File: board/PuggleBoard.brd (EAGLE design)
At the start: 54.6 x 86.4 mm, 140 parts, among them U1 OPA4209, U10 24C, U2 ADS8331, U3 AD5686, U4 OPA4209, U5 TPS7A3001, U6 TPS7A4901, U7 LTM8045, U8 REF5040, U9 AD8032

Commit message: Fixed several problems in grounding scheme causing digital/analog interference.
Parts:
- moved C16 3.61 mm to (7.87, 65.5), turned to 90 degrees
- moved C3 1.42 mm to (17.1, 42.7), turned to 180 degrees
- moved C4 1.25 mm to (16.9, 44.5), turned to 180 degrees
- moved C15 0.65 mm to (17.8, 63.6), turned to 270 degrees
- moved C1 0.57 mm to (10.7, 42.4), turned to 180 degrees
- moved C14 0.40 mm to (19.6, 63.9), turned to 270 degrees
- moved C2 0.13 mm to (10.8, 44.2), turned to 180 degrees
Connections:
- net +4.5V renamed N$27
- removed net DGND: BB1.48
- net GND: now also BB1.48
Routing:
- net VDRIVE: track 54.3 -> 26.1 mm
- net DGND: track 24.2 -> 0.00 mm, vias 1 -> 0
- net N$31: track 75.2 -> 65.7 mm
- net N$35: track 68.1 -> 60.5 mm
- net GND: track 117.9 -> 114.7 mm, vias 82 -> 84
- net DAC_+IN_C: track 37.4 -> 35.9 mm
- net N$27: track 42.5 -> 41.7 mm, vias 15 -> 16
- net SPI4: track 23.2 -> 23.8 mm
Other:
- board text added: "PuggleBoard v2.1 Aug. 2013"
- board text removed: "PuggleBoard v2.0 Aug. 2013"

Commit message: Fixed V_Ref bypass cap for DAC.
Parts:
- C21: value 0.1uF -> 10uF; device puggleboard:0603 -> puggleboard:0805
- moved C21 0.36 mm to (19.1, 59.3)

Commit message: Almost done with 2v0 board changes. Getting ready for 2.1 fabrication.
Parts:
- added C46: 22uF, puggleboard:1206
- U1: value OPA4209 -> LMP7704
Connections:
- net GND: now also C46.1
- net VDRIVE: now also C46.2
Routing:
- net GND: track 115.1 -> 116.6 mm, vias 84 -> 85
- net VDRIVE: track 26.1 -> 27.6 mm, vias 14 -> 15
- net N$20: track 12.9 -> 12.0 mm

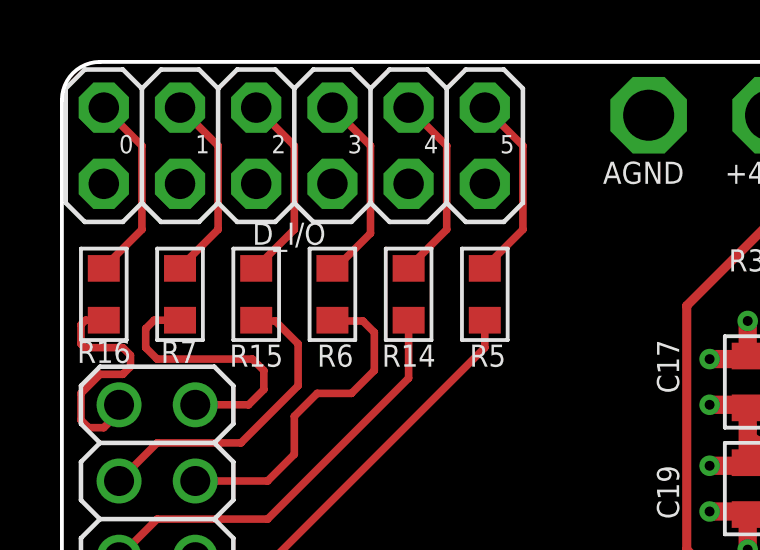
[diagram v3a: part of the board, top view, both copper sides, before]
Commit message: Changes to ground/vdrive planes.
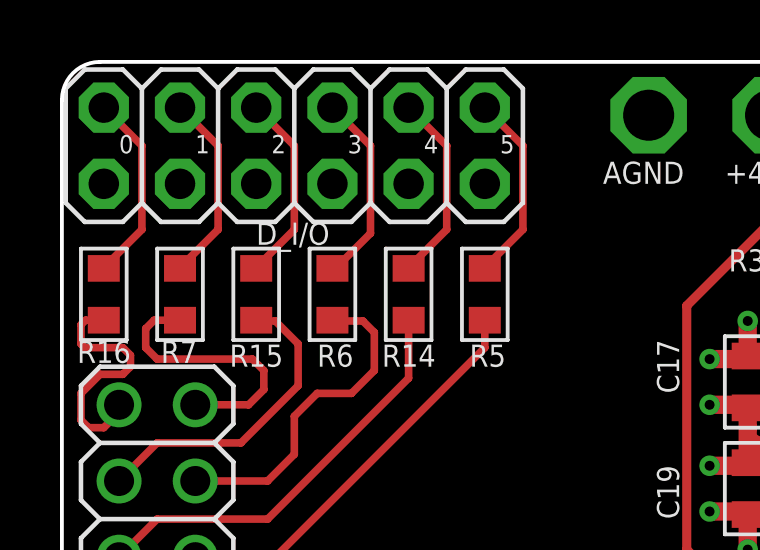
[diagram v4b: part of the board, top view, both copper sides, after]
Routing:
- net -4.5V: track 88.9 -> 88.2 mm
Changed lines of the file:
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@@
 </element>
 <element name="D_I/O" library="puggleboard" package="2X06" value="PINHD-2X6" x="7.747" y="83.566" smashed="yes">
-<attribute name="NAME" x="6.35" y="80.264" size="0.7366" layer="25" font="vector" ratio="12"/>
+<attribute name="NAME" x="6.477" y="80.264" size="0.7366" layer="25" font="vector" ratio="12"/>
 </element>
 <element name="U$1" library="puggleboard" package="PB-LOGO" value="" x="41.529" y="6.985"/>
@@
 <wire x1="44.45" y1="37.338" x2="47.625" y2="37.338" width="0.8128" layer="15"/>
 <wire x1="47.625" y1="37.338" x2="48.514" y2="38.354" width="0.8128" layer="15"/>
-<wire x1="48.514" y1="79.248" x2="47.879" y2="79.883" width="0.8128" layer="15"/>
-<wire x1="47.879" y1="79.883" x2="47.244" y2="80.518" width="0.8128" layer="15"/>
+<wire x1="48.514" y1="79.248" x2="47.752" y2="80.01" width="0.8128" layer="15"/>
+<wire x1="47.752" y1="80.01" x2="47.244" y2="80.518" width="0.8128" layer="15"/>
 <wire x1="47.244" y1="80.518" x2="43.053" y2="80.518" width="0.8128" layer="15"/>
 <via x="45.466" y="37.338" extent="1-16" drill="0.3302"/>
 <via x="46.482" y="37.338" extent="1-16" drill="0.3302"/>
-<wire x1="40.64" y1="80.518" x2="35.56" y2="80.518" width="0.8128" layer="15"/>
+<wire x1="40.64" y1="80.518" x2="36.322" y2="80.518" width="0.8128" layer="15"/>
+<wire x1="36.322" y1="80.518" x2="35.052" y2="79.248" width="0.8128" layer="15"/>
 <via x="34.29" y="72.898" extent="1-16" drill="0.3302"/>
 <via x="34.29" y="74.93" extent="1-16" drill="0.3302"/>
@@
 <wire x1="33.108" y1="72.898" x2="34.29" y2="72.898" width="0.6096" layer="1"/>
 <wire x1="34.29" y1="74.93" x2="33.02" y2="74.93" width="0.6096" layer="1"/>
-<wire x1="49.022" y1="81.788" x2="49.276" y2="81.28" width="0.3048" layer="15"/>
-<wire x1="49.276" y1="81.28" x2="47.879" y2="79.883" width="0.3048" layer="15"/>
 <via x="48.514" y="74.93" extent="1-16" drill="0.3302"/>
 <via x="48.514" y="72.898" extent="1-16" drill="0.3302"/>
@@
 <wire x1="40.64" y1="80.518" x2="43.053" y2="80.518" width="0.8128" layer="16"/>
 <via x="35.052" y="79.248" extent="1-16" drill="0.6"/>
-<wire x1="35.56" y1="80.518" x2="35.052" y2="80.01" width="0.8128" layer="15"/>
-<wire x1="35.052" y1="80.01" x2="35.052" y2="79.248" width="0.8128" layer="15"/>
 <wire x1="35.052" y1="79.248" x2="34.29" y2="78.486" width="0.8128" layer="16"/>
 <wire x1="34.29" y1="78.486" x2="34.29" y2="74.93" width="0.8128" layer="16"/>
 <wire x1="34.29" y1="74.93" x2="34.29" y2="72.898" width="0.8128" layer="16"/>
+<wire x1="49.022" y1="81.788" x2="49.022" y2="81.28" width="0.4064" layer="15"/>
+<wire x1="49.022" y1="81.28" x2="47.752" y2="80.01" width="0.4064" layer="15"/>
 </signal>
 <signal name="VDRIVE">
@@
 <vertex x="0" y="86.106"/>
 <vertex x="0.254" y="86.36"/>
-<vertex x="15.748" y="86.36"/>
-<vertex x="15.748" y="68.072"/>
-<vertex x="12.7" y="65.024"/>
+<vertex x="16.002" y="86.36"/>
+<vertex x="16.002" y="64.897"/>
+<vertex x="13.6919" y="64.897"/>
+<vertex x="12.7" y="63.9051"/>
 <vertex x="12.7" y="55.372"/>
 <vertex x="13.97" y="53.975"/>
@@
 <via x="27.051" y="22.479" extent="1-16" drill="0.6"/>
 <contactref element="C46" pad="2"/>
-<wire x1="8.382" y1="26.3144" x2="8.382" y2="26.162" width="0" layer="19" extent="1-1"/>
 <wire x1="27.051" y1="22.479" x2="25.527" y2="22.479" width="1.016" layer="1"/>
+<wire x1="8.382" y1="26.162" x2="8.382" y2="26.3144" width="0" layer="19" extent="1-1"/>
 </signal>
 <signal name="VDD_5V">
@@
 <polygon width="0.254" layer="2" thermals="no">
 <vertex x="0.127" y="86.36"/>
+<vertex x="16.002" y="86.36"/>
+<vertex x="16.002" y="73.406"/>
+<vertex x="10.549153125" y="67.953153125" curve="135"/>
+<vertex x="10.710346875" y="67.564" curve="44.999782"/>
+<vertex x="11.121625" y="67.73435625"/>
+<vertex x="16.637" y="73.24973125"/>
+<vertex x="16.637" y="86.36"/>
 <vertex x="46.001321875" y="86.36"/>
 <vertex x="49.022" y="83.339321875"/>
@@
 <vertex x="54.61" y="0"/>
 <vertex x="33.655" y="0"/>
-<vertex x="33.655" y="18.161"/>
-<vertex x="47.498" y="18.161"/>
+<vertex x="33.655" y="18.034"/>
+<vertex x="47.625" y="18.034"/>
 <vertex x="49.022" y="16.637"/>
 <vertex x="51.308" y="16.637"/>
@@
 <vertex x="27.305" y="37.973"/>
 <vertex x="17.399" y="37.973"/>
-<vertex x="15.24" y="40.132"/>
-<vertex x="15.113" y="40.132"/>
-<vertex x="14.732" y="39.751"/>
-<vertex x="14.732" y="39.624"/>
+<vertex x="15.405453125" y="39.966546875" curve="90"/>
+<vertex x="14.947546875" y="39.966546875" curve="90"/>
+<vertex x="14.947546875" y="39.408453125"/>
 <vertex x="17.018" y="37.338"/>
 <vertex x="27.051" y="37.338"/>
@@
 <vertex x="50.673" y="17.526"/>
 <vertex x="49.022" y="17.526"/>
-<vertex x="47.879" y="18.796"/>
+<vertex x="47.752" y="18.796"/>
 <vertex x="33.655" y="18.796"/>
 <vertex x="33.655" y="20.32"/>
@@
 <via x="20.701" y="22.479" extent="1-16" drill="0.6"/>
 <contactref element="C46" pad="1"/>
+<wire x1="20.701" y1="22.479" x2="22.225" y2="22.479" width="1.016" layer="1"/>
 <wire x1="52.705" y1="72.39" x2="52.705" y2="74.93" width="0" layer="19" extent="1-1"/>
 <wire x1="50.165" y1="74.93" x2="52.705" y2="74.93" width="0" layer="19" extent="1-1"/>
@@
 <wire x1="9.8806" y1="65.024" x2="9.906" y2="65.024" width="0" layer="19" extent="1-1"/>
 <wire x1="46.99" y1="71.2724" x2="46.99" y2="71.374" width="0" layer="19" extent="1-1"/>
-<wire x1="20.701" y1="22.479" x2="22.225" y2="22.479" width="1.016" layer="1"/>
 </signal>
 <signal name="BAT_SENSE">
@@
 <wire x1="43.942" y1="57.658" x2="44.196" y2="57.912" width="0.6096" layer="1"/>
 <polygon width="0.254" layer="15" thermals="no">
-<vertex x="16.256" y="86.36"/>
+<vertex x="16.637" y="86.36"/>
 <vertex x="46.001321875" y="86.36"/>
 <vertex x="49.022" y="83.339321875"/>
@@
 <vertex x="26.76168125" y="39.979434375"/>
 <vertex x="15.138565625" y="39.979434375"/>
-<vertex x="14.478" y="40.64"/>
-<vertex x="14.478" y="43.815"/>
+<vertex x="14.351" y="40.767"/>
+<vertex x="14.351" y="43.942"/>
 <vertex x="12.192" y="46.228"/>
 <vertex x="12.192" y="49.53"/>
@@
 <vertex x="14.478" y="54.102"/>
 <vertex x="13.208" y="55.499"/>
-<vertex x="13.208" y="64.77"/>
-<vertex x="16.256" y="67.818"/>
+<vertex x="13.208" y="63.70280625"/>
+<vertex x="13.89419375" y="64.389"/>
+<vertex x="16.637" y="64.389"/>
 </polygon>
 <wire x1="44.577" y1="57.023" x2="44.196" y2="56.642" width="0.6096" layer="1"/>

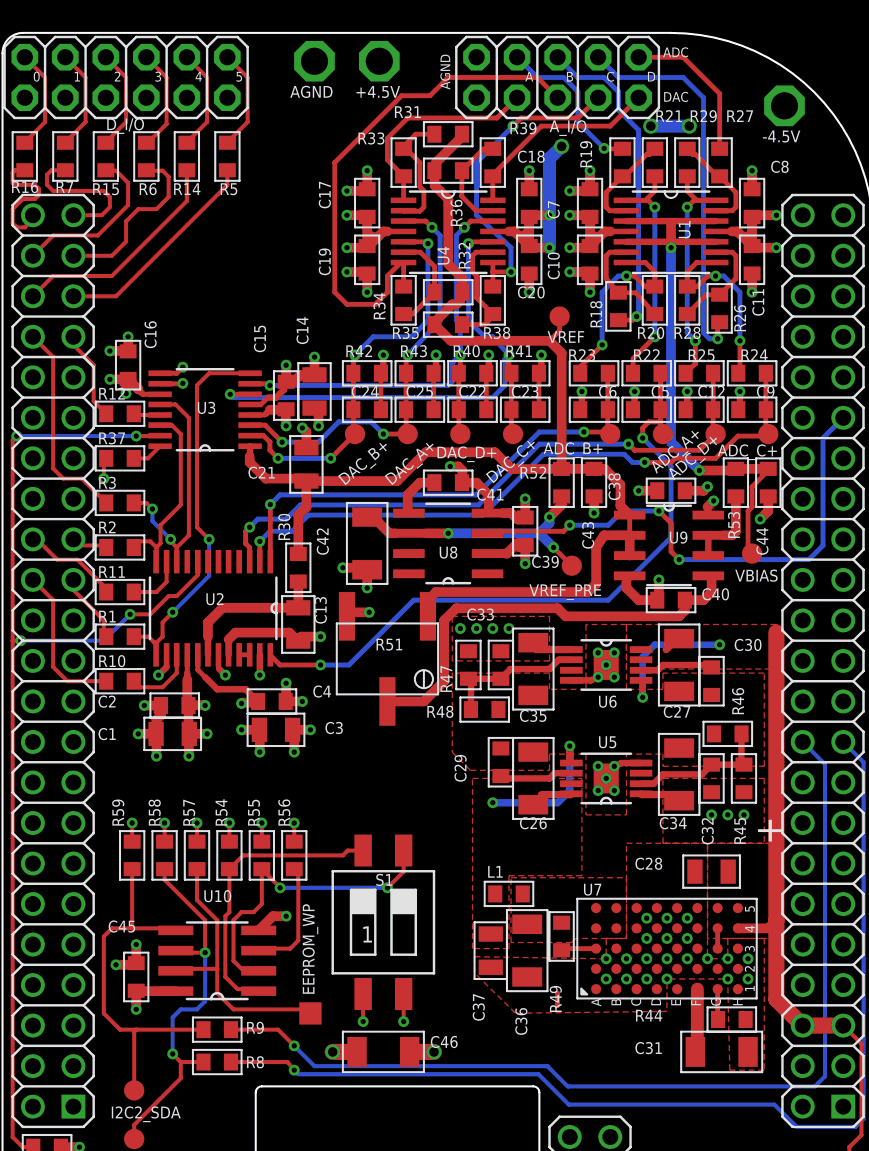
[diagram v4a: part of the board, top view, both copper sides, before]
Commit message: PuggleBoard version 2.1. Created gerbers and placed order.
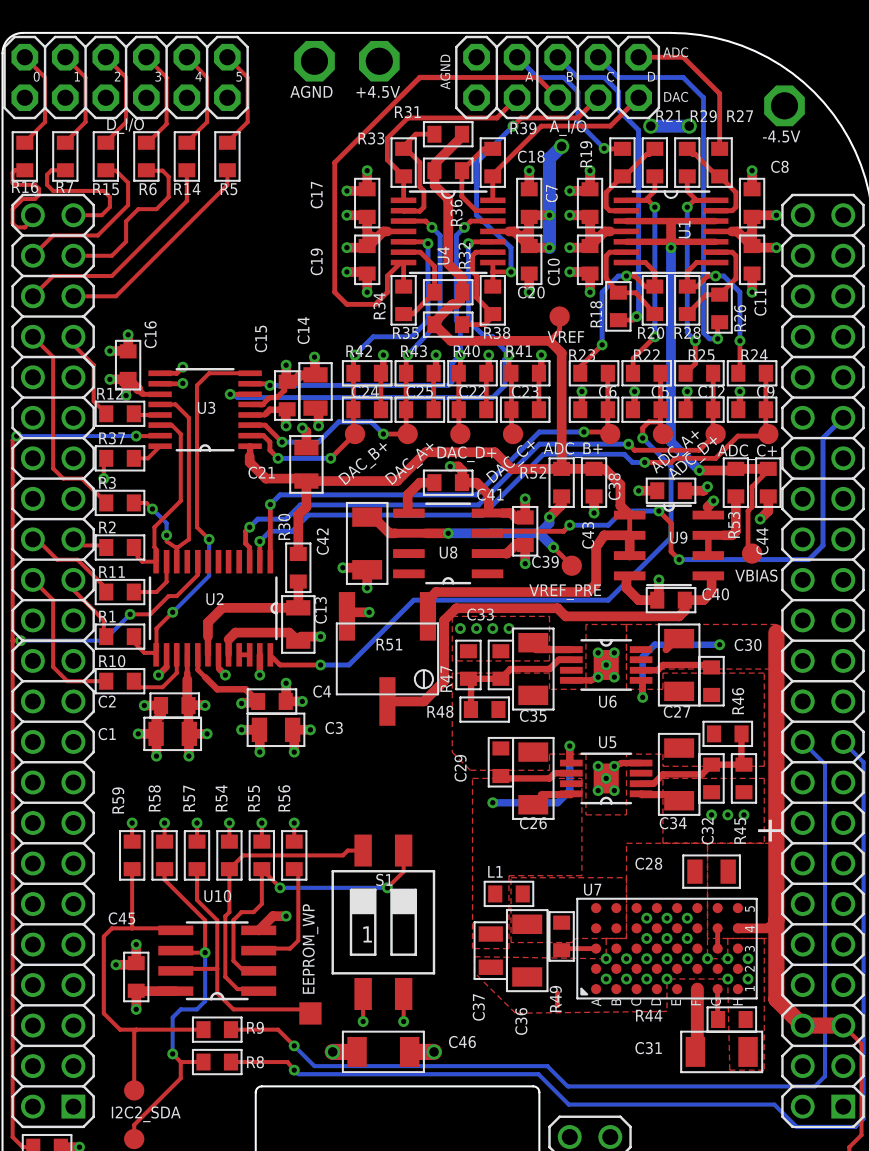
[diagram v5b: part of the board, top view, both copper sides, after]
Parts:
- moved U$2 2.67 mm to (31.2, 27.3)
- moved C14 0.06 mm to (19.6, 63.9)
- moved C15 0.06 mm to (17.8, 63.6)
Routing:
- net SPI3: track 12.1 -> 13.1 mm

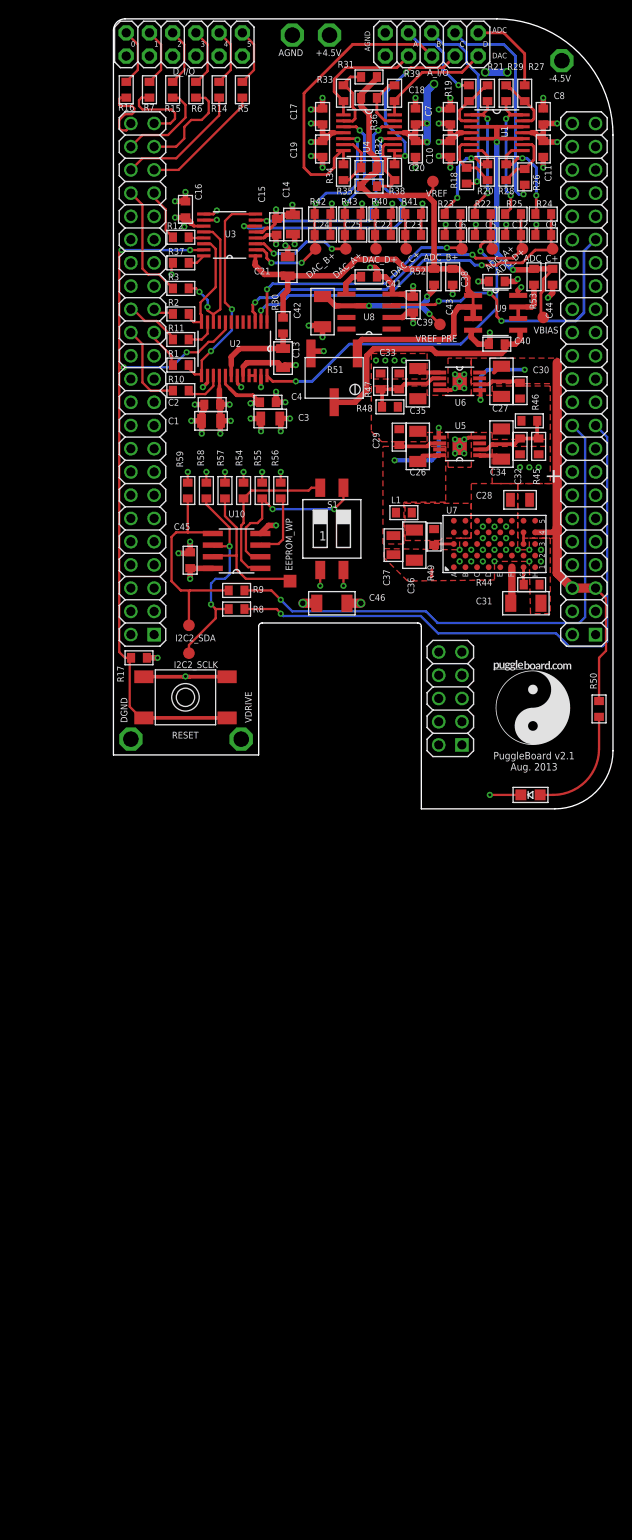
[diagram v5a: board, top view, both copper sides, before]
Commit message: Started fixing issues with r2.1 build. Fixed up silkscreen to make it more legible. Fixed issue with voltage ref miswiring.
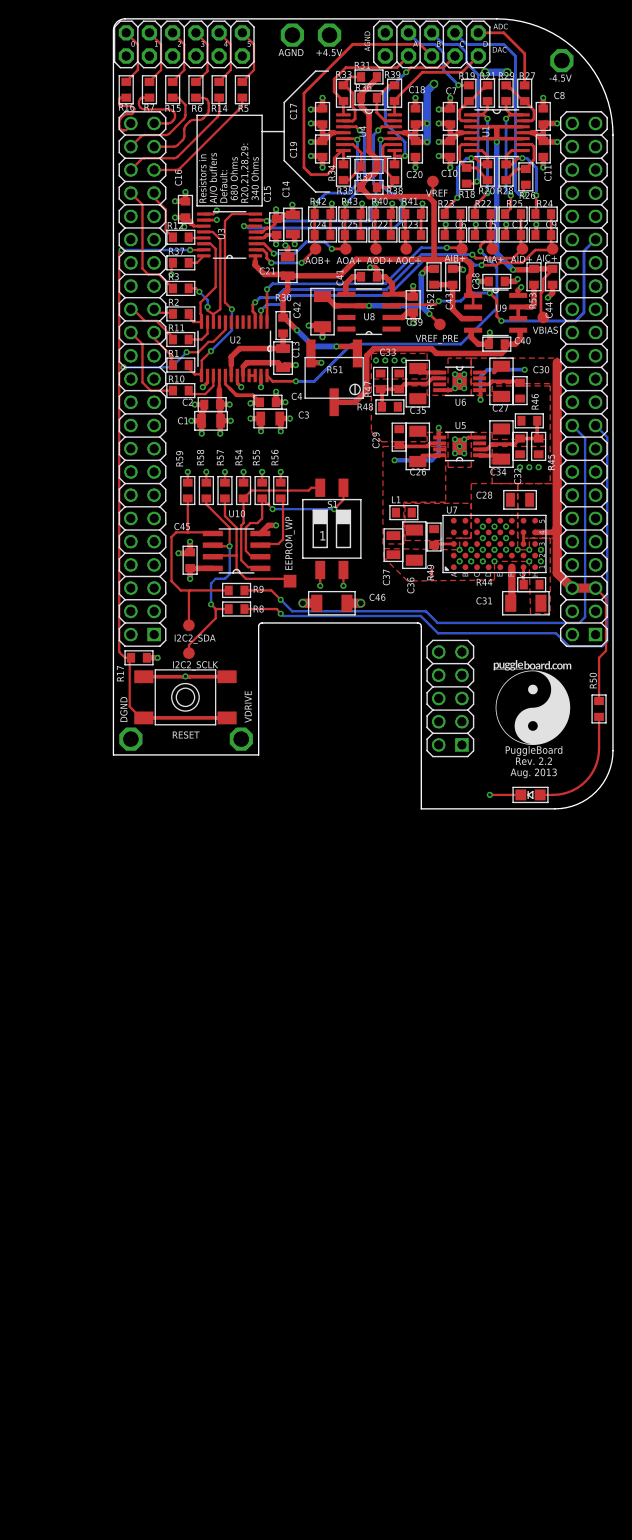
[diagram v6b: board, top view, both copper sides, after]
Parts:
- moved R35 0.13 mm to (27.9, 67.9)
- moved R26 0.13 mm to (45.1, 69.1)
- moved R32 0.13 mm to (27.9, 70.2)
- turned C43 to 90 degrees
- turned R52 to 90 degrees
- renumbered ADC_A+ to AIA+, ADC_B+ to AIB+, ADC_C+ to AIC+, ADC_D+ to AID+, DAC_A+ to AOA+, DAC_B+ to AOB+, DAC_C+ to AOC+, DAC_D+ to AOD+
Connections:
- net N$27 renamed +4.5V
- new net N$28: C43.1, R52.1, U9.3
- net VREF: no longer C43.1, R52.1, U9.3
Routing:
- net N$28: track 0.00 -> 7.38 mm
- net VREF: track 84.9 -> 77.7 mm, vias 0 -> 2
- net VREF_PRE: track 17.3 -> 19.5 mm
- net GND: track 116.7 -> 117.5 mm
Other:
- board text added: "PuggleBoard Rev. 2.2 Aug. 2013"
- board text added: "Resistors in AI/O buffers Default: 680 Ohms R20,21,28,29: 340 Ohms"
- board text removed: "+"
- board text removed: "PuggleBoard v2.1 Aug. 2013"

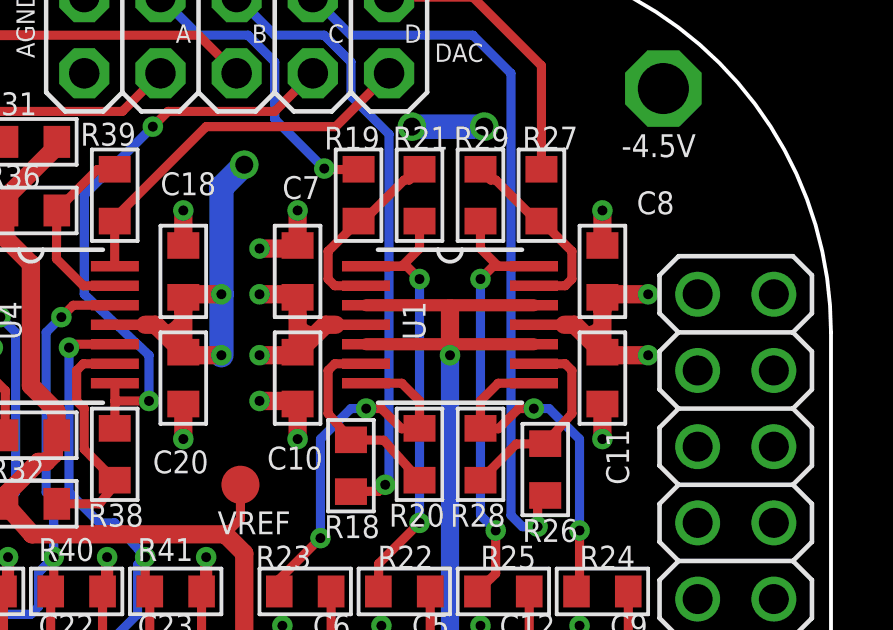
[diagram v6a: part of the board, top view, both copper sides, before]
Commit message: Started documenting and addressing Edgar's comments.
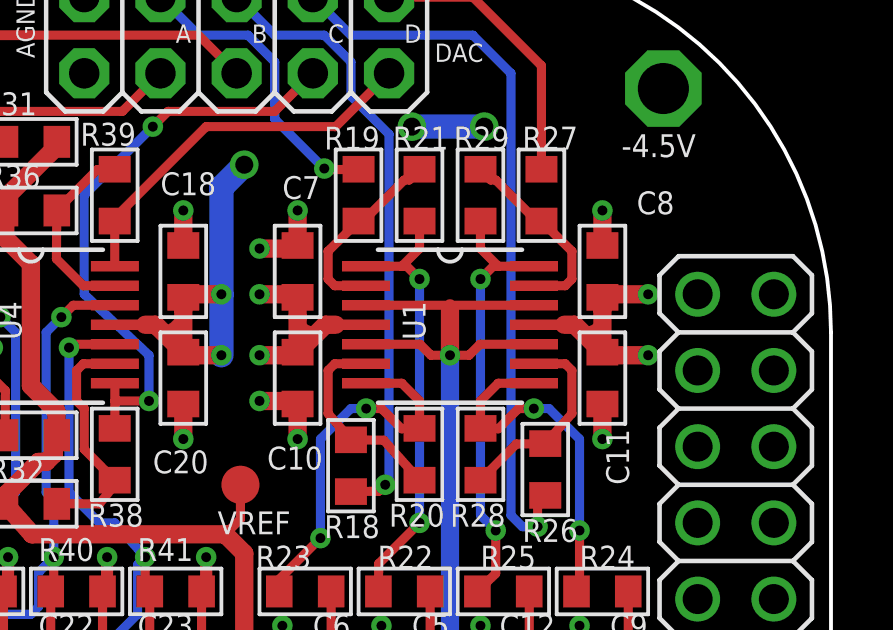
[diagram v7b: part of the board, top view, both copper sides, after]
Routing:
- net ADC_D+: track 15.8 -> 14.6 mm
- net ADC_A+: track 15.9 -> 14.7 mm
